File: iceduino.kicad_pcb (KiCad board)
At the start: 4 copper layers, 80 x 100 mm, 243 parts, among them J1 7-17 V IN, J2 USB_B_Micro, J3 Conn_01x08, J4 Conn_01x06, J5 Conn_01x10, J6 Conn_01x08, Q1 DMP3099L-7, Q2 Q_NMOS_GSD, Q3 Q_NMOS_GSD, Q4 Q_NMOS_GSD, SW1 SW_Push, SW2 SW_Push, SW3 SW_Push, SW4 SW_Push, SW5 SW_Push, SW6 JS202011SCQN, SW7 JS202011SCQN, SW8 SW_Push, SW9 JS202011SCQN, U1 ICE40HX4K-TQ144, U10 MAX40200AUK, U11 MAX40200AUK, U12 TXS0108EPW, U13 MAX11614, U14 TXS0108EPW, U15 93LCxxBT-I_OT, U16 FT2232H, U17 SN74LVC1G32DBVR, U18 SN74LVC2T45DCUR, U19 SN74LVC2T45DCUR, U2 MAX40200AUK, U20 SN74AXC4T245PWR, U21 SN74LVC2T45DCUR, U22 SN74LVC2T45DCUR, U23 SN74LVC2G07DCKR, U24 IS25LP080D, U3 TPS562201, U4 MAX40200AUK, U5 MAX40200AUK, U6 TLV62568APDRLR, U7 TLV62568APDRLR, U8 IS61WV5128EDBLL-10TLI, U9 MIC5365-3.3YC5, Y1 ECS-3225S33-500-FN-TR, Y2 ECS-3225S33-120-FN-TR

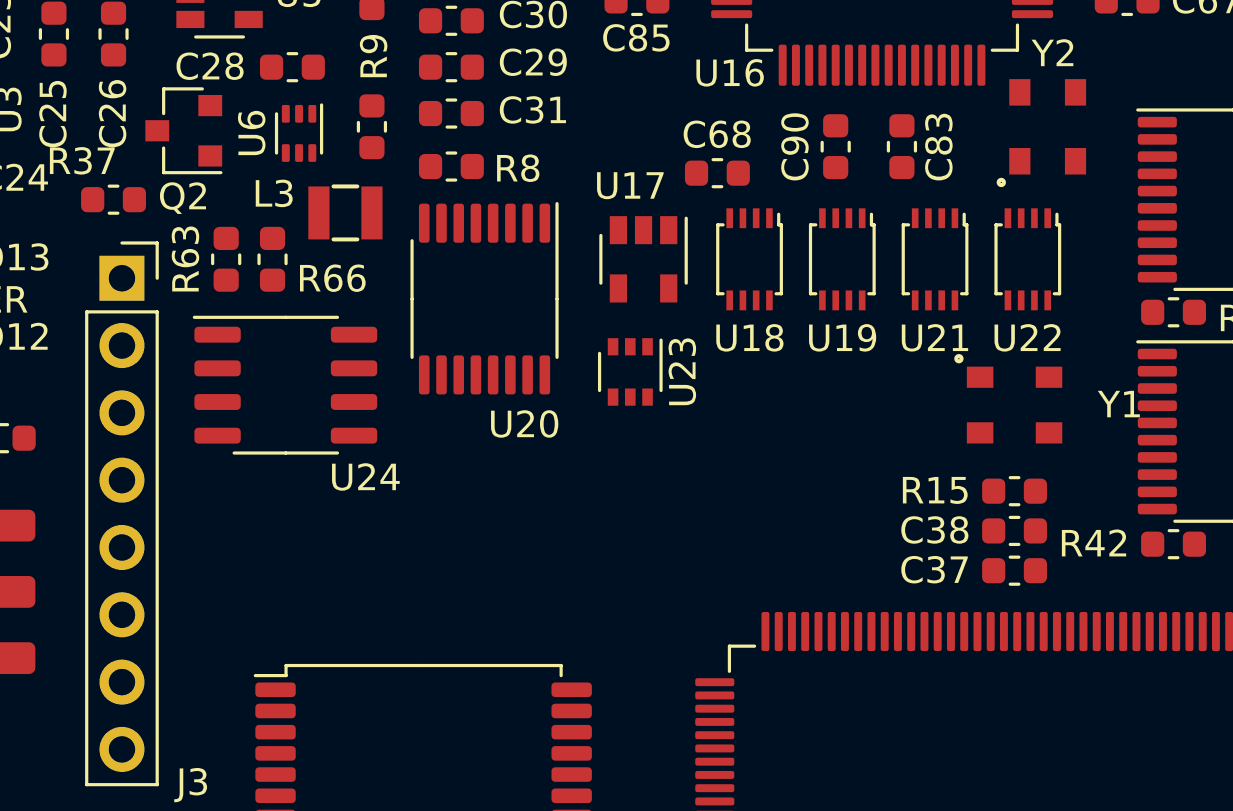
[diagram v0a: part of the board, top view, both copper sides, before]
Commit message: 8MBit Flash swapped to a 64MBit one
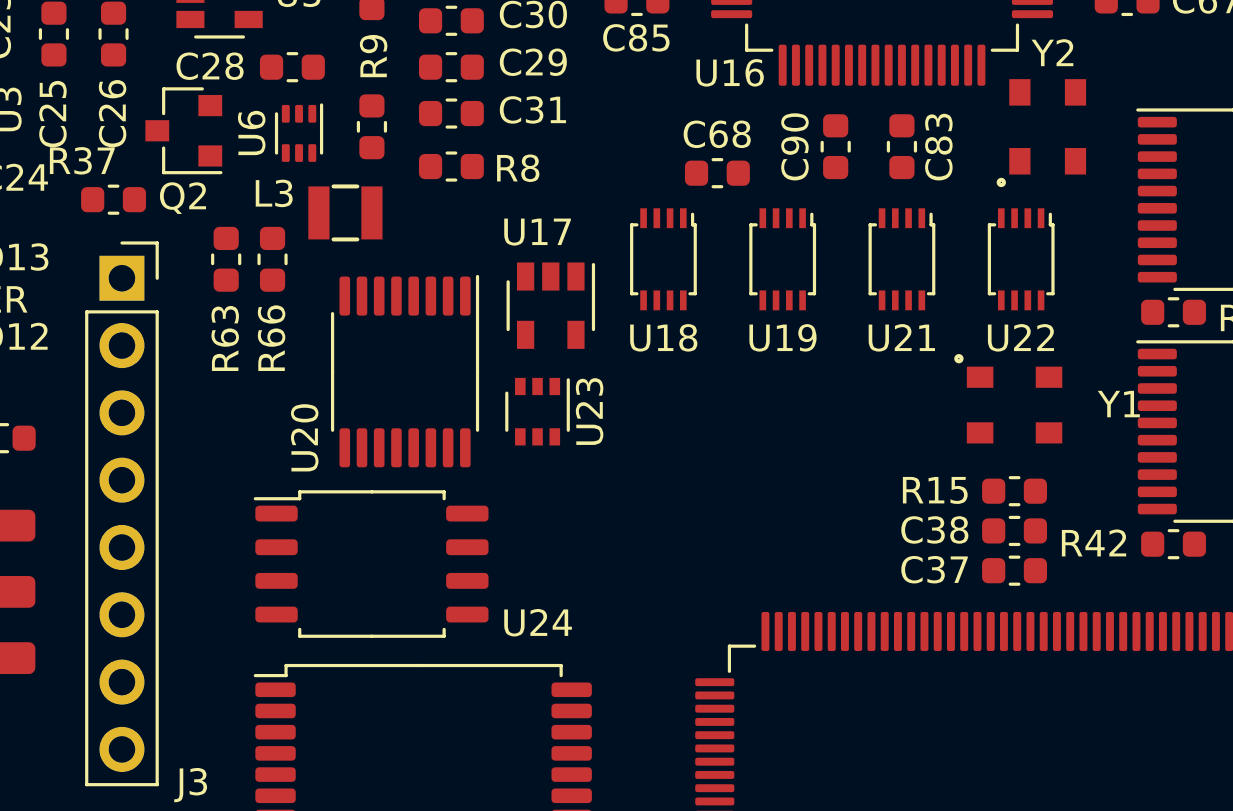
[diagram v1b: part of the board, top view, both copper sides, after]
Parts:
- U24: value IS25LP080D -> W25Q64JV; footprint Package_SO:SO-8_3.9x4.9mm_P1.27mm -> Package_SO:SOIC-8_5.23x5.23mm_P1.27mm
- moved U24 7.49 mm to (64.5, 84.8)
- moved U20 4.07 mm to (65.8, 77.5)
- moved U17 3.91 mm to (71.2, 75.0)
- moved U23 3.81 mm to (70.8, 79.0)
- moved U18 3.25 mm to (75.5, 73.2)
- moved U19 2.25 mm to (80.0, 73.2)
- moved U21 1.25 mm to (84.5, 73.2)
- moved U22 0.25 mm to (89.0, 73.2)

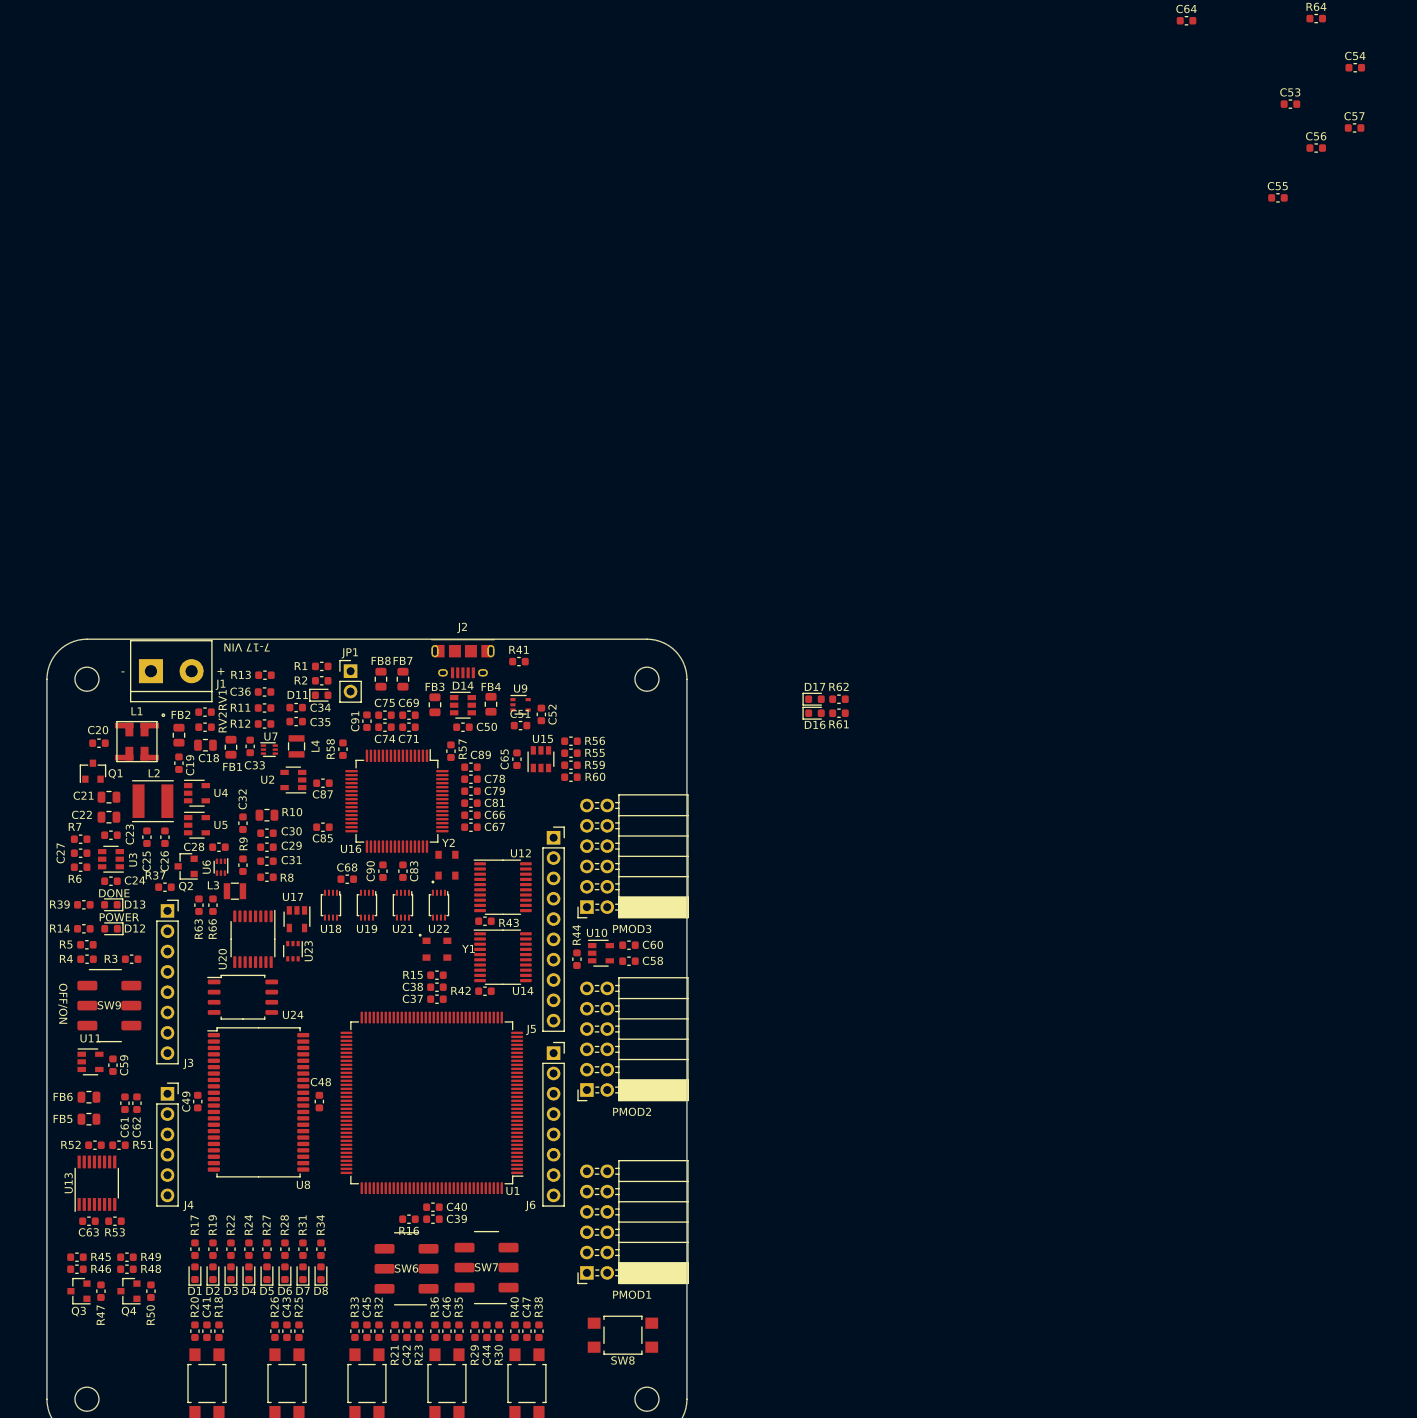
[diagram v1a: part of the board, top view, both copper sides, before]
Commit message: 7-17 VIN Power PIN Header moved to the left for better compatibility with extension boards. Added 0 Ohm resistors for optional desoldering of quad-SPI wires. USB power jumper moved more to the side of the board. Arduino Header decoupling capacitors moved to arduino header sheet.
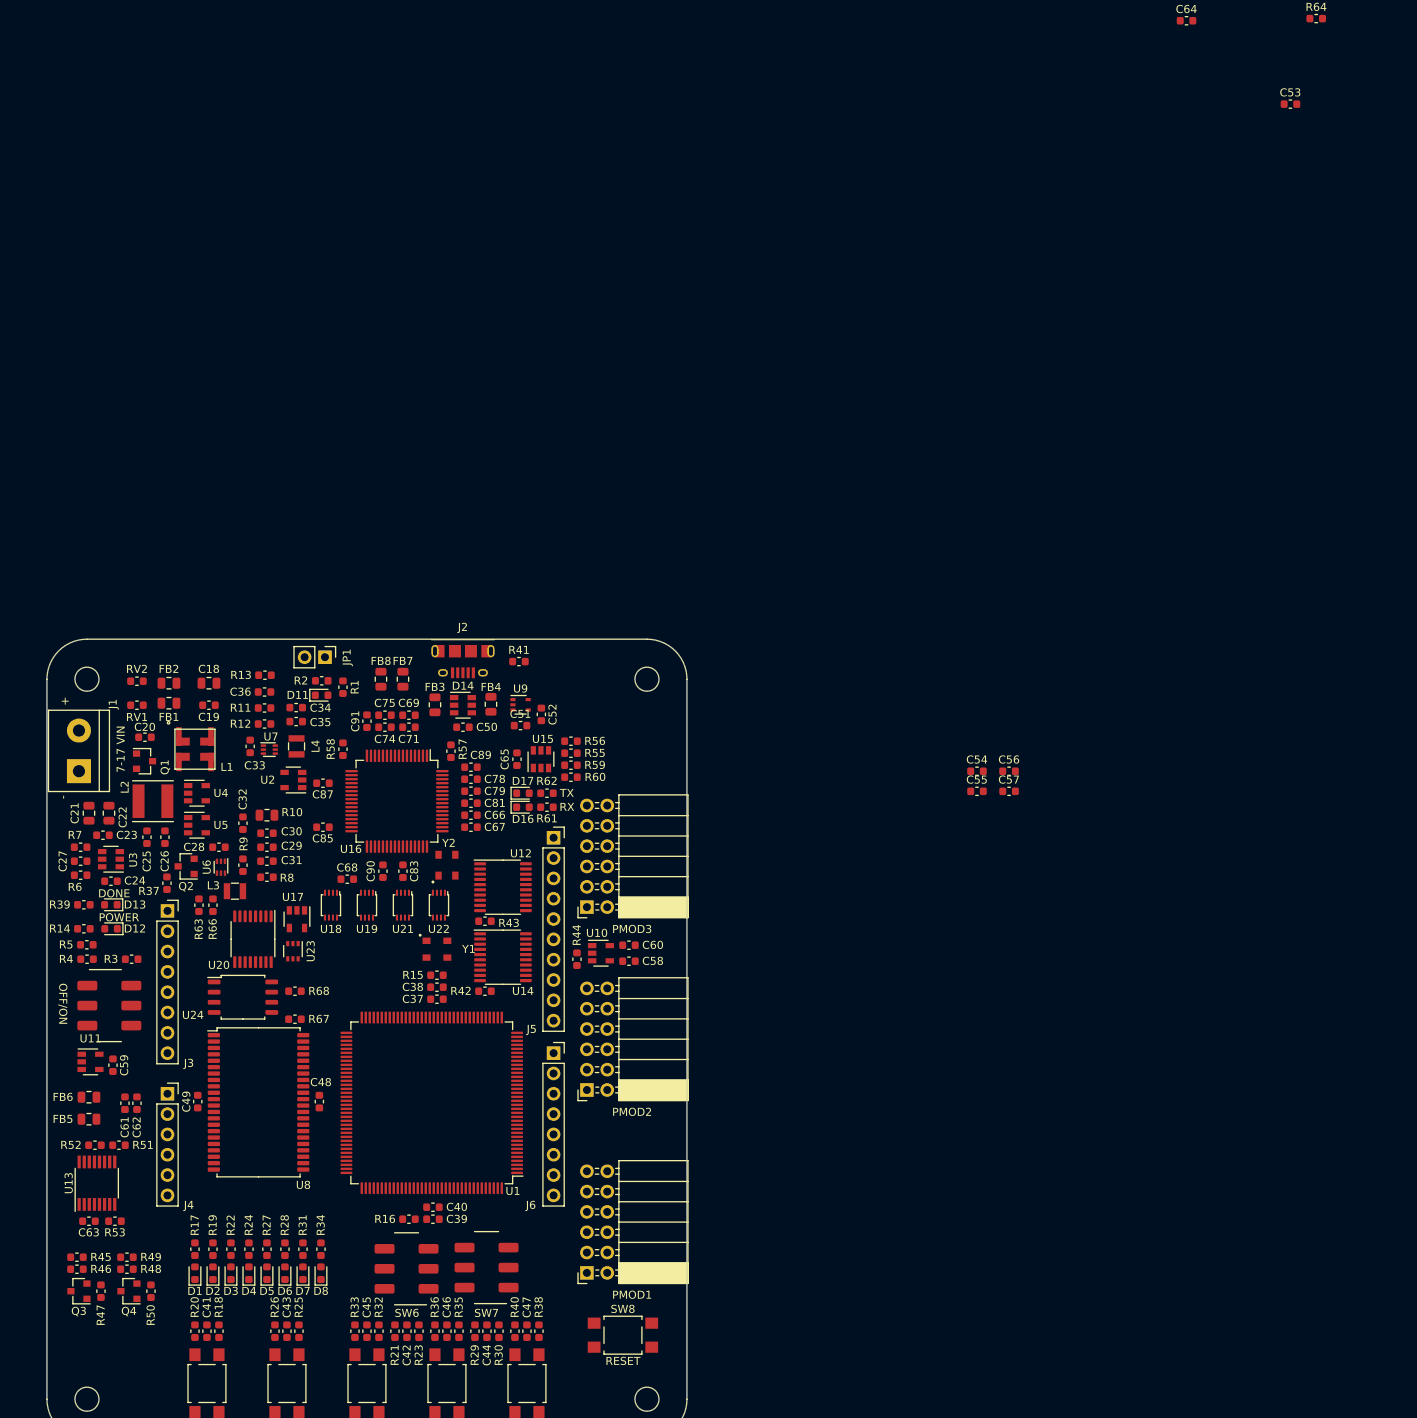
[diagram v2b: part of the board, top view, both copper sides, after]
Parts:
- added R67: 0, Resistor_SMD:R_0603_1608Metric, F.Cu at (71.0, 87.5)
- added R68: 0, Resistor_SMD:R_0603_1608Metric, F.Cu at (71.0, 84.0)
- moved C54 99.8 mm to (156.3, 56.5)
- moved C57 93.5 mm to (160.3, 59.0)
- moved C56 86.8 mm to (160.3, 56.5)
- moved C55 83.2 mm to (156.3, 59.0)
- moved D16 38.3 mm to (99.5, 61.0)
- moved D17 38.3 mm to (99.5, 59.2)
- moved R61 38.3 mm to (102.5, 61.0)
- moved R62 38.3 mm to (102.5, 59.2)
- moved J1 15.4 mm to (44.0, 56.5), turned to 90 degrees
- moved RV2 10.3 mm to (51.2, 45.2), turned to 0 degrees
- moved FB1 9.50 mm to (55.2, 48.0), turned to 180 degrees
- moved RV1 8.55 mm to (51.2, 48.2), turned to 0 degrees
- moved C19 8.16 mm to (60.2, 48.2), turned to 0 degrees
- moved C18 7.76 mm to (60.2, 45.5), turned to 0 degrees
- moved L1 7.31 mm to (58.5, 53.8), turned to 0 degrees
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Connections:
- net /MISO renamed /FLASH_IO1
- net /MOSI renamed /FLASH_IO0
- C54 pad 1: +3V3 -> /HEADER/INO_3V3
- C55 pad 1: +3V3 -> /HEADER/INO_3V3
- U1 pad 63: Net-(U1-Pad63) -> /FLASH_IO3
- U1 pad 64: Net-(U1-Pad64) -> /FLASH_IO2
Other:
- board text added: "RESET"
- board text added: "RX"
- board text added: "TX"

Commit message: Move of decoupling capacitors from last commit reverted (meant for Arduino Header Level Shifters). Component placement complete.
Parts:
- C1, C10, C11, C12, C13, C14, C15, C16, C17, C2, C3, C37, C38, C39, C4, C40, C48, C49, C5, C6, C7, C8, C9, R15, R16: moved to B.Cu
- moved D10 265.5 mm to (77.2, 109.2)
- moved D9 262.5 mm to (48.2, 78.2), turned to 180 degrees
- moved C12 241.8 mm to (96.0, 94.5), turned to 270 degrees
- moved C5 241.6 mm to (90.5, 112.2), turned to 270 degrees
- moved C4 241.1 mm to (96.2, 103.5), turned to 90 degrees
- moved C6 240.8 mm to (86.2, 112.2), turned to 270 degrees
- moved C14 237.5 mm to (81.2, 105.5)
- moved C11 234.0 mm to (88.8, 98.2), turned to 180 degrees
- moved C3 233.4 mm to (96.0, 91.2), turned to 90 degrees
- moved C10 232.9 mm to (92.5, 83.5), turned to 90 degrees
- moved C9 232.1 mm to (87.0, 83.5), turned to 90 degrees
- moved C1 230.9 mm to (92.2, 94.0), turned to 180 degrees
- moved C17 229.8 mm to (94.0, 91.2), turned to 270 degrees
- moved C7 227.7 mm to (81.5, 100.8)
- moved C8 225.8 mm to (81.5, 97.0)
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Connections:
- C54 pad 1: /HEADER/INO_3V3 -> +3V3
- C55 pad 1: /HEADER/INO_3V3 -> +3V3
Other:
- board text added: "USB POWER"
